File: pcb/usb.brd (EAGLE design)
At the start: 26.2 x 26.2 mm, 26 parts, among them J1 JSTPH, Q1 ZXMP6A13FTA, Q2 mmbt2222, Q3 mmbt2222, U1 MIC5225-3.3v, U2 CH340C, U3 MCP73831T-2ACI/OT

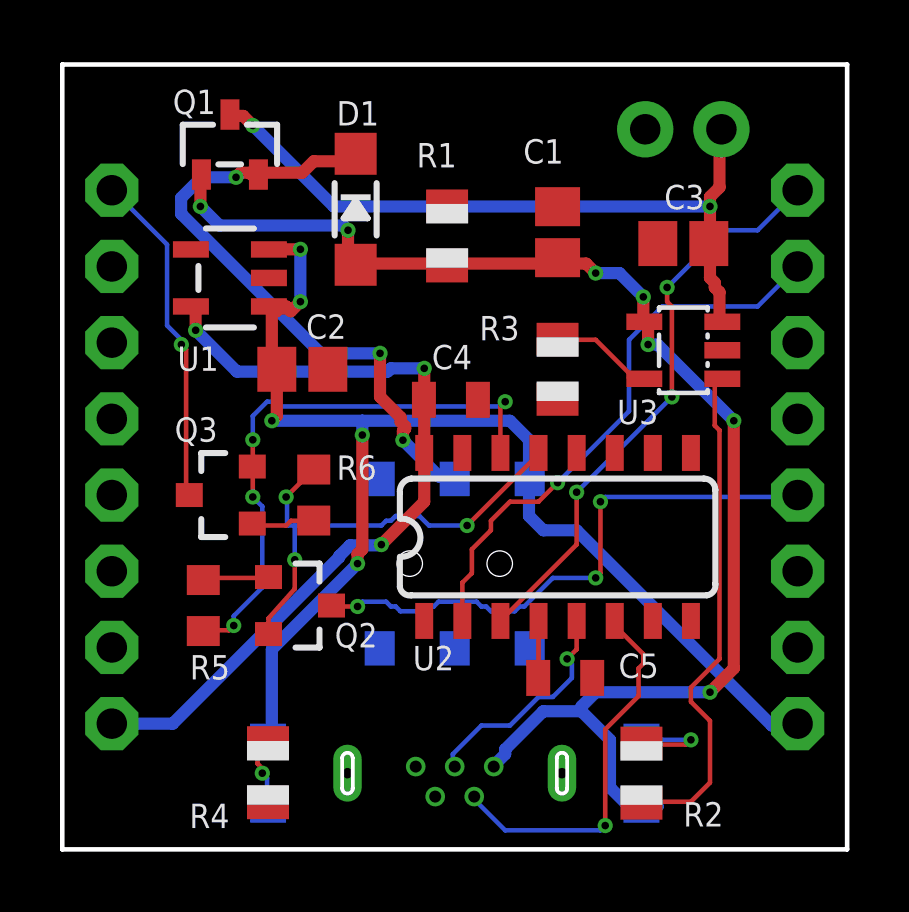
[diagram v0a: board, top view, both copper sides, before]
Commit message: Add jumper to bypass switch on USB board
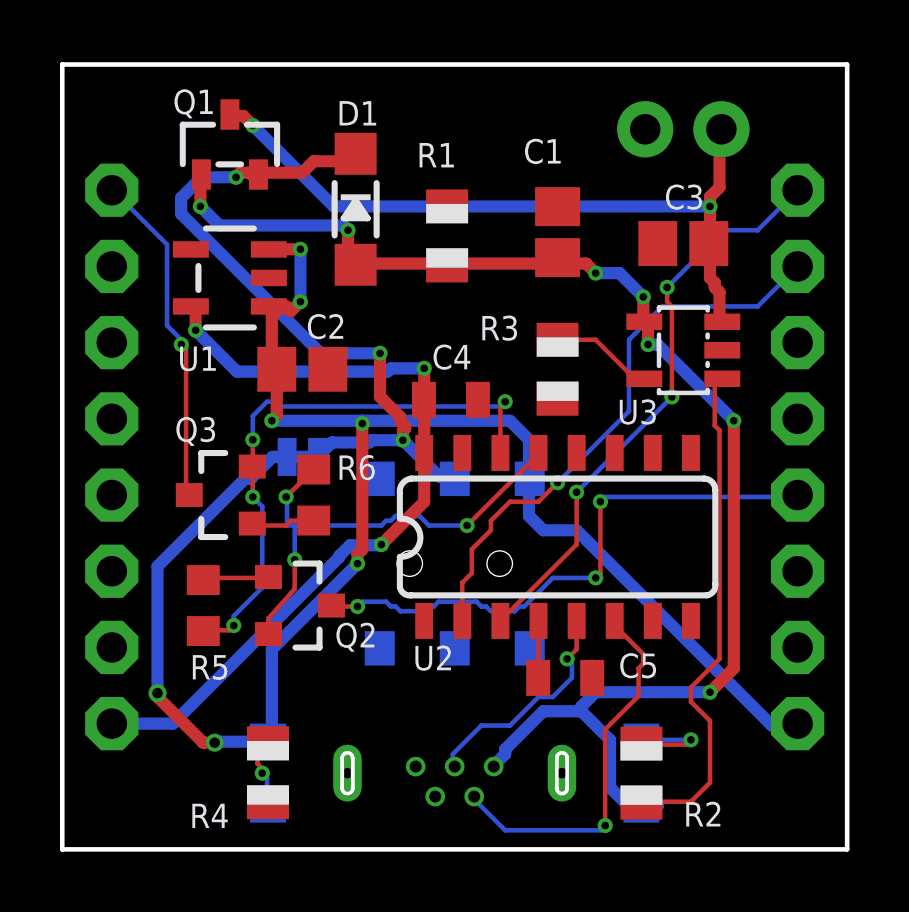
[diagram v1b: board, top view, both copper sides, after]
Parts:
- added JP3: Switch Bypass, SparkFun-Jumpers:SMT-JUMPER_2_NC_TRACE_NO-SILK
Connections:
- net N$7: now also JP3.1
- net VIN: now also JP3.2
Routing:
- net VIN: track 43.5 -> 59.0 mm, vias 5 -> 7
- net N$7: track 21.1 -> 24.2 mm
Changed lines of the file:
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@@
 </element>
 <element name="U$1" library="Twitter" package="TWITTER5MM" value="" x="15.113" y="18.542" smashed="yes" rot="MR0"/>
+<element name="JP3" library="SparkFun-Jumpers" library_urn="urn:adsk.eagle:library:528" package="SMT-JUMPER_2_NC_TRACE_NO-SILK" package3d_urn="urn:adsk.eagle:package:39286/1" value="Switch Bypass" x="8.001" y="13.081" smashed="yes" rot="MR0">
+<attribute name="NAME" x="8.509" y="14.097" size="0.8128" layer="26" font="vector" rot="MR0" align="bottom-center"/>
+<attribute name="VALUE" x="8.001" y="11.938" size="0.6096" layer="28" font="vector" ratio="20" rot="MR0" align="top-center"/>
+</element>
 </elements>
 <signals>
@@
 <via x="10.5918" y="16.5354" extent="1-16" drill="0.254"/>
 <via x="5.7912" y="22.4028" extent="1-16" drill="0.254"/>
+<contactref element="JP3" pad="1"/>
+<wire x1="11.3538" y1="13.6398" x2="10.31090625" y2="13.6398" width="0.4064" layer="16"/>
+<wire x1="10.23470625" y1="13.5636" x2="10.31090625" y2="13.6398" width="0.4064" layer="16"/>
+<wire x1="8.509" y1="13.081" x2="8.9916" y2="13.5636" width="0.4064" layer="16"/>
+<wire x1="8.9916" y1="13.5636" x2="10.23470625" y2="13.5636" width="0.4064" layer="16"/>
 </signal>
 <signal name="VIN" class="1">
@@
 <wire x1="9.8425" y1="9.8425" x2="9.8425" y2="9.525" width="0.4064" layer="1"/>
 <wire x1="10.00125" y1="10.00125" x2="9.8425" y2="9.8425" width="0.4064" layer="1"/>
-<wire x1="10.00125" y1="13.81125" x2="10.00125" y2="10.00125" width="0.4064" layer="1"/>
-<wire x1="10.00125" y1="14.2875" x2="10.00125" y2="13.81125" width="0.4064" layer="16"/>
+<wire x1="10.00125" y1="14.19225" x2="10.00125" y2="10.00125" width="0.4064" layer="1"/>
+<wire x1="10.00125" y1="14.2875" x2="10.00125" y2="14.19225" width="0.4064" layer="16"/>
 <wire x1="6.985" y1="3.65125" x2="6.858" y2="3.59" width="0.4064" layer="16"/>
 <wire x1="6.985" y1="17.93875" x2="6.8881" y2="18.097" width="0.4064" layer="1"/>
@@
 <via x="6.985" y="14.2875" extent="1-16" drill="0.254"/>
 <via x="9.8425" y="9.525" extent="1-16" drill="0.254"/>
-<via x="10.00125" y="13.81125" extent="1-16" drill="0.254"/>
+<via x="10.00125" y="14.19225" extent="1-16" drill="0.254"/>
 <via x="7.9375" y="20.0025" extent="1-16" drill="0.254"/>
 <via x="7.9375" y="18.25625" extent="1-16" drill="0.254"/>
@@
 <wire x1="7.151" y1="16.002" x2="7.151" y2="14.4535" width="0.4064" layer="1"/>
 <wire x1="7.151" y1="14.4535" x2="6.985" y2="14.2875" width="0.4064" layer="1"/>
+<contactref element="JP3" pad="2"/>
+<wire x1="6.858" y1="3.59" x2="5.114" y2="3.59" width="0.4064" layer="16"/>
+<wire x1="5.114" y1="3.59" x2="5.08" y2="3.556" width="0.4064" layer="16"/>
+<via x="5.08" y="3.556" extent="1-16" drill="0.35"/>
+<wire x1="5.08" y1="3.556" x2="4.699" y2="3.556" width="0.4064" layer="1"/>
+<wire x1="4.699" y1="3.556" x2="3.175" y2="5.08" width="0.4064" layer="1"/>
+<wire x1="3.175" y1="5.08" x2="3.175" y2="5.207" width="0.4064" layer="1"/>
+<via x="3.175" y="5.207" extent="1-16" drill="0.35"/>
+<wire x1="6.09749375" y1="12.3571" x2="6.2865" y2="12.3571" width="0.4064" layer="16"/>
+<wire x1="7.0104" y1="13.081" x2="6.2865" y2="12.3571" width="0.4064" layer="16"/>
+<wire x1="3.175" y1="5.207" x2="3.175" y2="9.43460625" width="0.4064" layer="16"/>
+<wire x1="3.175" y1="9.43460625" x2="6.09749375" y2="12.3571" width="0.4064" layer="16"/>
+<wire x1="7.493" y1="13.081" x2="7.0104" y2="13.081" width="0.4064" layer="16"/>
+<wire x1="7.493" y1="13.081" x2="8.509" y2="13.081" width="0.4064" layer="16"/>
 </signal>
 <signal name="N$2">
@@
 <mfgpreviewcolor name="substratecolor" color="0xFF786E46"/>
 </mfgpreviewcolors>
+<errors>
+</errors>
 </board>
 </drawing>

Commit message: Make the slots for the usb connector wider
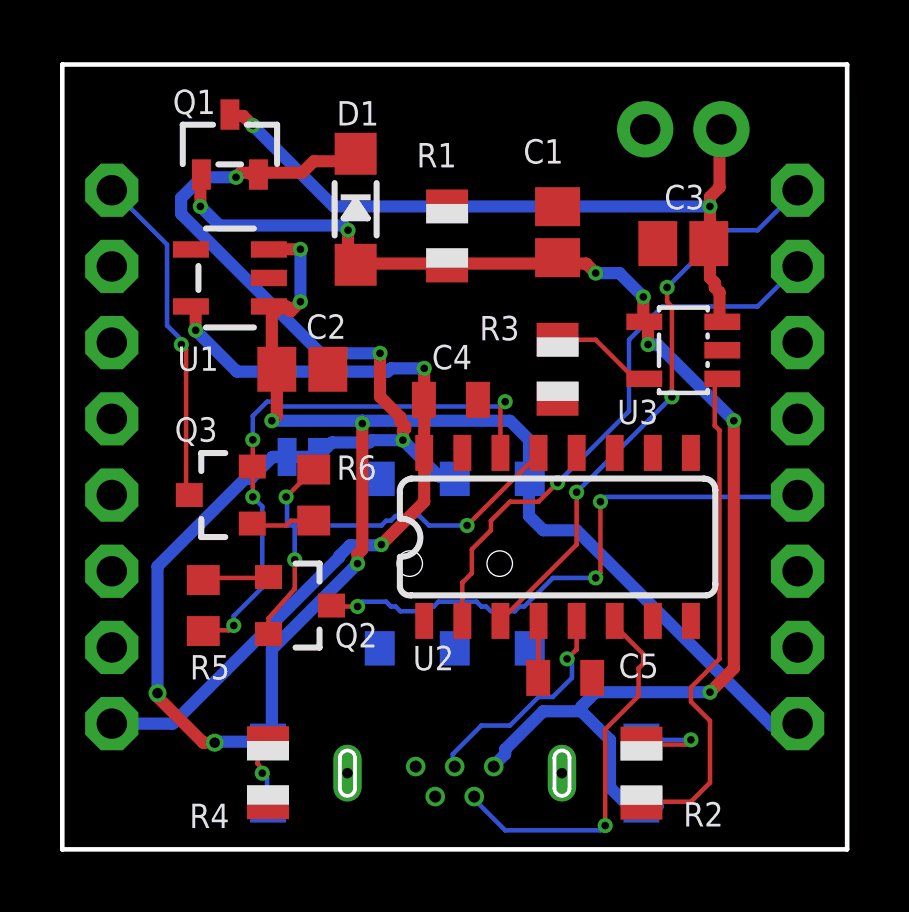
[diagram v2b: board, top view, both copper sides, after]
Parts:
- J2: device Wurth_Elektronik_Electromechanic_Input-Output_Connectors_rev19b:614105150621 -> Wurth_Elektronik_Electromechanic_Input-Output_Connectors_rev19b_wider_slots:614105150621
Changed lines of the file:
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@@
 <layer number="44" name="Drills" color="7" fill="1" visible="no" active="yes"/>
 <layer number="45" name="Holes" color="7" fill="1" visible="no" active="yes"/>
-<layer number="46" name="Milling" color="3" fill="1" visible="no" active="yes"/>
+<layer number="46" name="Milling" color="3" fill="1" visible="yes" active="yes"/>
 <layer number="47" name="Measures" color="7" fill="1" visible="no" active="yes"/>
 <layer number="48" name="Document" color="7" fill="1" visible="no" active="yes"/>
@@
 <attribute name="VALUE" x="27.686" y="23.241" size="1.27" layer="28" rot="MR270"/>
 </element>
-<element name="J2" library="Wurth_Elektronik_Electromechanic_Input-Output_Connectors_rev19b" library_urn="urn:adsk.eagle:library:488835" package="614105150621" package3d_urn="urn:adsk.eagle:package:3360156/4" value="" x="13.081" y="2.54" smashed="yes" rot="MR0">
+<element name="J2" library="Wurth_Elektronik_Electromechanic_Input-Output_Connectors_rev19b_wider_slots" package="614105150621" package3d_urn="urn:adsk.eagle:package:3360156/4" value="" x="13.081" y="2.54" smashed="yes" rot="MR0">
 <attribute name="MPN" value="614105150621" x="13.081" y="2.54" size="1.778" layer="28" rot="MR0" display="off"/>
 <attribute name="VALUE" x="15.6726" y="-0.61" size="1.016" layer="28" font="vector" ratio="13" rot="SMR0"/>

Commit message: Remove switch bypass jumper (revert c81c233)
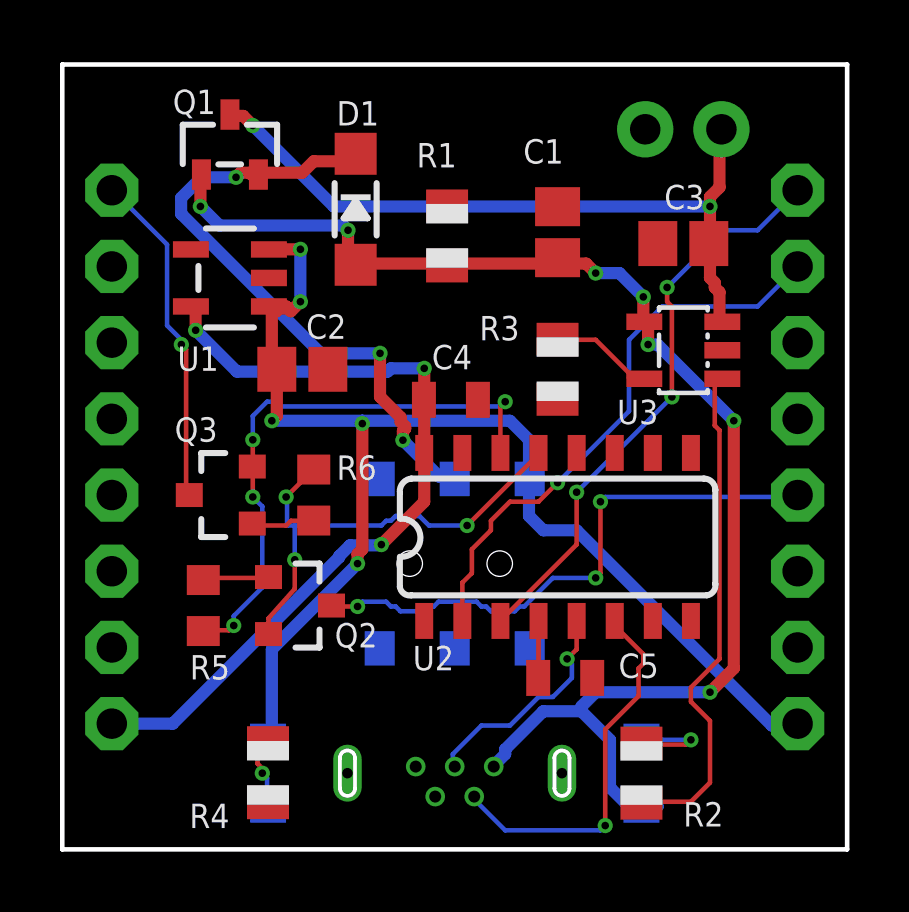
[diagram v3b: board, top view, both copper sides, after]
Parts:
- removed JP3: Switch Bypass, SparkFun-Jumpers:SMT-JUMPER_2_NC_TRACE_NO-SILK
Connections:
- net N$7: no longer JP3.1
- net VIN: no longer JP3.2
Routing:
- net VIN: track 59.0 -> 43.5 mm, vias 7 -> 5
- net N$7: track 24.2 -> 21.1 mm
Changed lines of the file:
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@@
 <layer number="44" name="Drills" color="7" fill="1" visible="no" active="yes"/>
 <layer number="45" name="Holes" color="7" fill="1" visible="no" active="yes"/>
-<layer number="46" name="Milling" color="3" fill="1" visible="yes" active="yes"/>
+<layer number="46" name="Milling" color="3" fill="1" visible="no" active="yes"/>
 <layer number="47" name="Measures" color="7" fill="1" visible="no" active="yes"/>
 <layer number="48" name="Document" color="7" fill="1" visible="no" active="yes"/>
@@
 </element>
 <element name="U$1" library="Twitter" package="TWITTER5MM" value="" x="15.113" y="18.542" smashed="yes" rot="MR0"/>
-<element name="JP3" library="SparkFun-Jumpers" library_urn="urn:adsk.eagle:library:528" package="SMT-JUMPER_2_NC_TRACE_NO-SILK" package3d_urn="urn:adsk.eagle:package:39286/1" value="Switch Bypass" x="8.001" y="13.081" smashed="yes" rot="MR0">
-<attribute name="NAME" x="8.509" y="14.097" size="0.8128" layer="26" font="vector" rot="MR0" align="bottom-center"/>
-<attribute name="VALUE" x="8.001" y="11.938" size="0.6096" layer="28" font="vector" ratio="20" rot="MR0" align="top-center"/>
-</element>
 </elements>
 <signals>
@@
 <via x="10.5918" y="16.5354" extent="1-16" drill="0.254"/>
 <via x="5.7912" y="22.4028" extent="1-16" drill="0.254"/>
-<contactref element="JP3" pad="1"/>
-<wire x1="11.3538" y1="13.6398" x2="10.31090625" y2="13.6398" width="0.4064" layer="16"/>
-<wire x1="10.23470625" y1="13.5636" x2="10.31090625" y2="13.6398" width="0.4064" layer="16"/>
-<wire x1="8.509" y1="13.081" x2="8.9916" y2="13.5636" width="0.4064" layer="16"/>
-<wire x1="8.9916" y1="13.5636" x2="10.23470625" y2="13.5636" width="0.4064" layer="16"/>
 </signal>
 <signal name="VIN" class="1">
@@
 <wire x1="7.151" y1="16.002" x2="7.151" y2="14.4535" width="0.4064" layer="1"/>
 <wire x1="7.151" y1="14.4535" x2="6.985" y2="14.2875" width="0.4064" layer="1"/>
-<contactref element="JP3" pad="2"/>
-<wire x1="6.858" y1="3.59" x2="5.114" y2="3.59" width="0.4064" layer="16"/>
-<wire x1="5.114" y1="3.59" x2="5.08" y2="3.556" width="0.4064" layer="16"/>
-<via x="5.08" y="3.556" extent="1-16" drill="0.35"/>
-<wire x1="5.08" y1="3.556" x2="4.699" y2="3.556" width="0.4064" layer="1"/>
-<wire x1="4.699" y1="3.556" x2="3.175" y2="5.08" width="0.4064" layer="1"/>
-<wire x1="3.175" y1="5.08" x2="3.175" y2="5.207" width="0.4064" layer="1"/>
-<via x="3.175" y="5.207" extent="1-16" drill="0.35"/>
-<wire x1="6.09749375" y1="12.3571" x2="6.2865" y2="12.3571" width="0.4064" layer="16"/>
-<wire x1="7.0104" y1="13.081" x2="6.2865" y2="12.3571" width="0.4064" layer="16"/>
-<wire x1="3.175" y1="5.207" x2="3.175" y2="9.43460625" width="0.4064" layer="16"/>
-<wire x1="3.175" y1="9.43460625" x2="6.09749375" y2="12.3571" width="0.4064" layer="16"/>
-<wire x1="7.493" y1="13.081" x2="7.0104" y2="13.081" width="0.4064" layer="16"/>
-<wire x1="7.493" y1="13.081" x2="8.509" y2="13.081" width="0.4064" layer="16"/>
 </signal>
 <signal name="N$2">
@@
 <mfgpreviewcolor name="substratecolor" color="0xFF786E46"/>
 </mfgpreviewcolors>
-<errors>
-</errors>
 </board>
 </drawing>

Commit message: Add a jst-sh battery connector
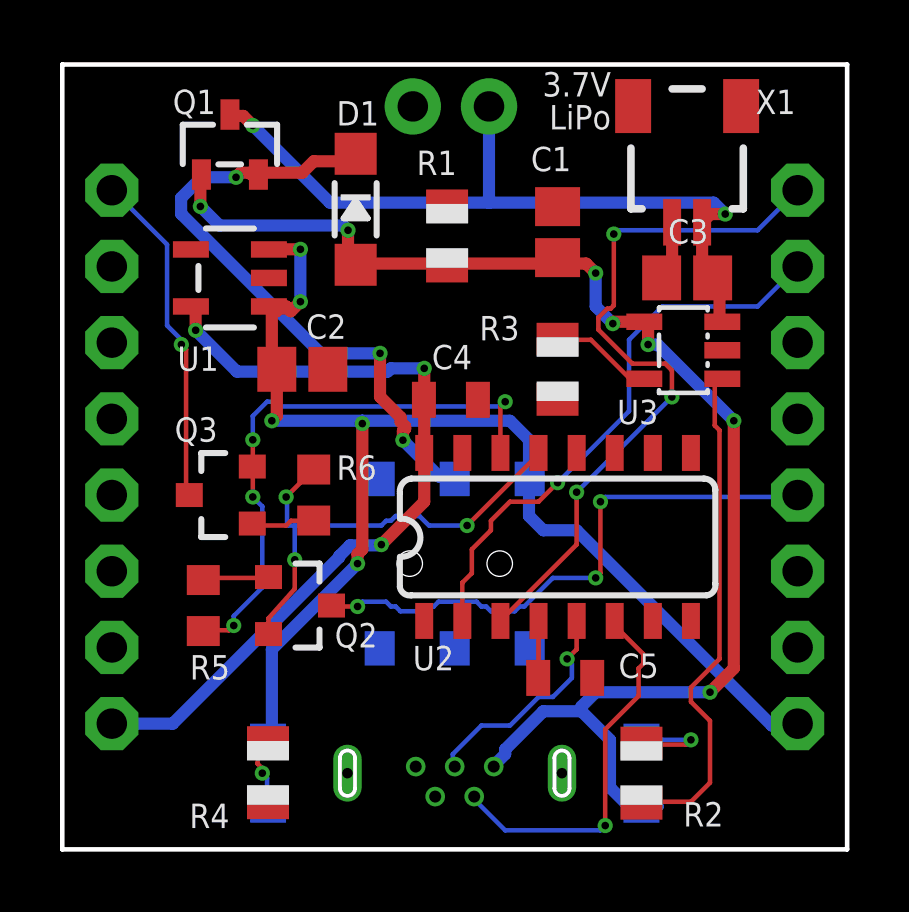
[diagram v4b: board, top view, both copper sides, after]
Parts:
- added X1: SM02B-SRSS-TB, con-jst2.rpt:SM02B-SRSS-TB
- moved J1 7.78 mm to (14.2, 24.8)
- moved C3 1.15 mm to (20.8, 19.1)
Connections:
- net GND: now also X1.2
- net V_BATT: now also X1.1
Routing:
- net TX: track 19.3 -> 24.0 mm
- net V_BATT: track 24.1 -> 26.2 mm
- net GND: track 0.00 -> 2.00 mm
